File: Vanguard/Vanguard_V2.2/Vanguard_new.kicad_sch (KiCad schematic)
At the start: 75 parts, among them J1 USB_C_Receptacle_USB2.0_16P, J2 Conn_02x03_Pin, J3 Micro_SD_Card_Det1, J4 STARBOARD_SERVO, J5 PORTSIDE_SERVO, J6 Conn_01x02_Pin, Q1 BSS138, Q2 BSS138, Q3 BSS138, Q4 BSS138, U1 ATSAMD11D14A-M, U2 ATmega4809-A, U3 AT25DF641A-SH-T, U4 AP2112K-3.3, U5 BD1020HFV, U6 BNO086, U7 TXB0104D, U8 TPS61092, U9 MPM3610AGQV-P, Y1 32.768kHz

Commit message: Debugged some errors
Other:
- note added: "note servo isnt connected"
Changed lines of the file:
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@@
+		)
+	)
+	(text "note servo isnt connected"
+		(exclude_from_sim no)
+		(at 339.344 189.992 0)
+		(effects
+			(font
+				(size 1.27 1.27)
+			)
 		)
 	)

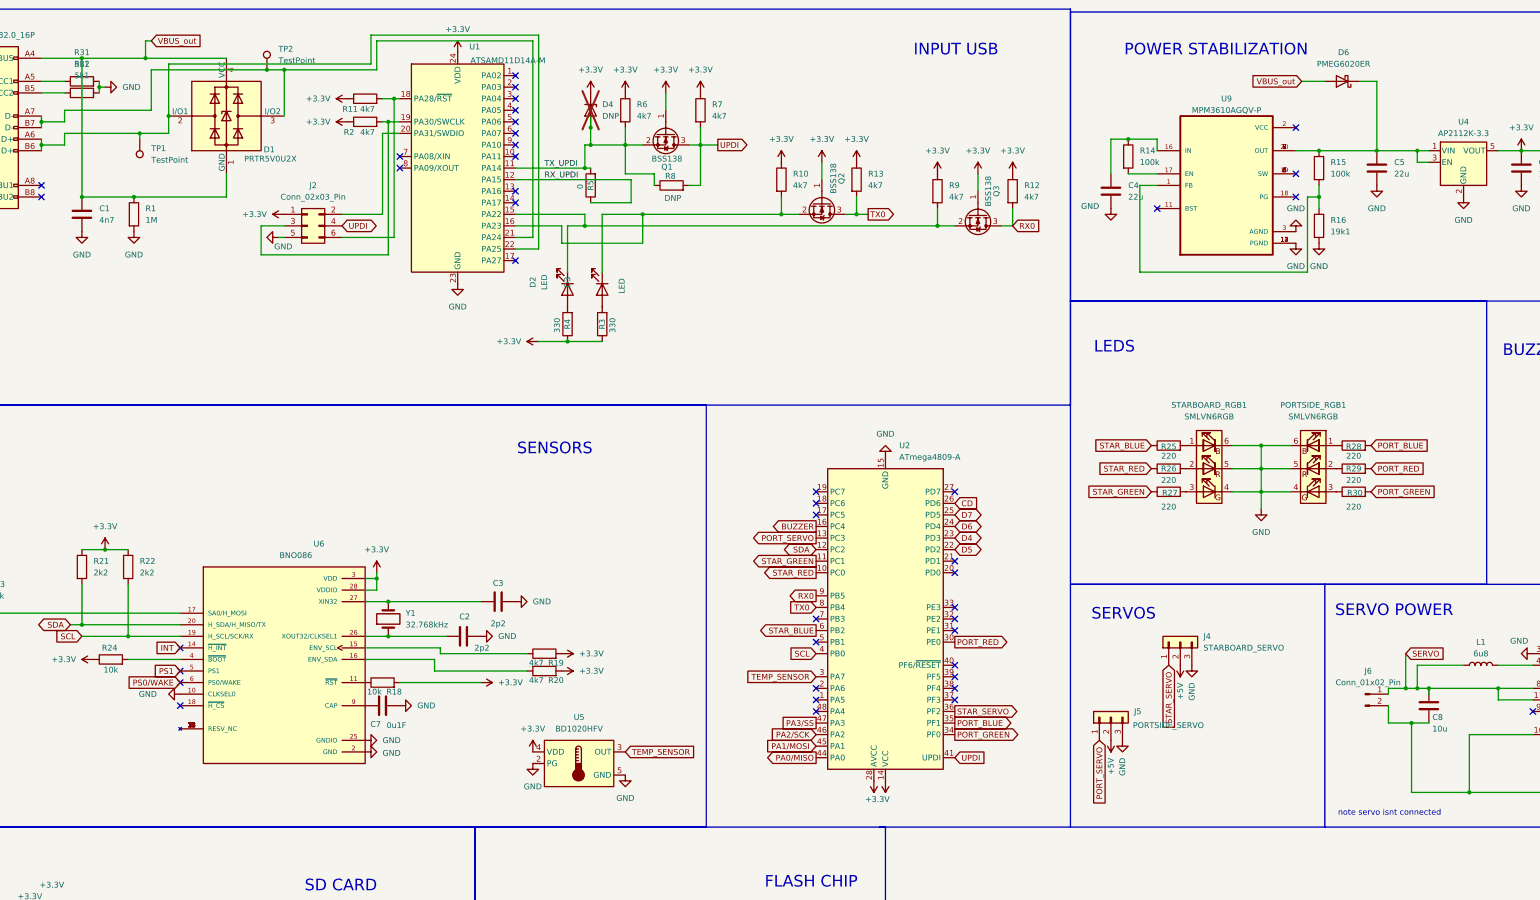
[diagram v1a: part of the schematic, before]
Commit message: Small erc changes as the pcb guys recommeded
@pchou05 @stygmatic what do you say? I am done with the sch but we still have some silly violations
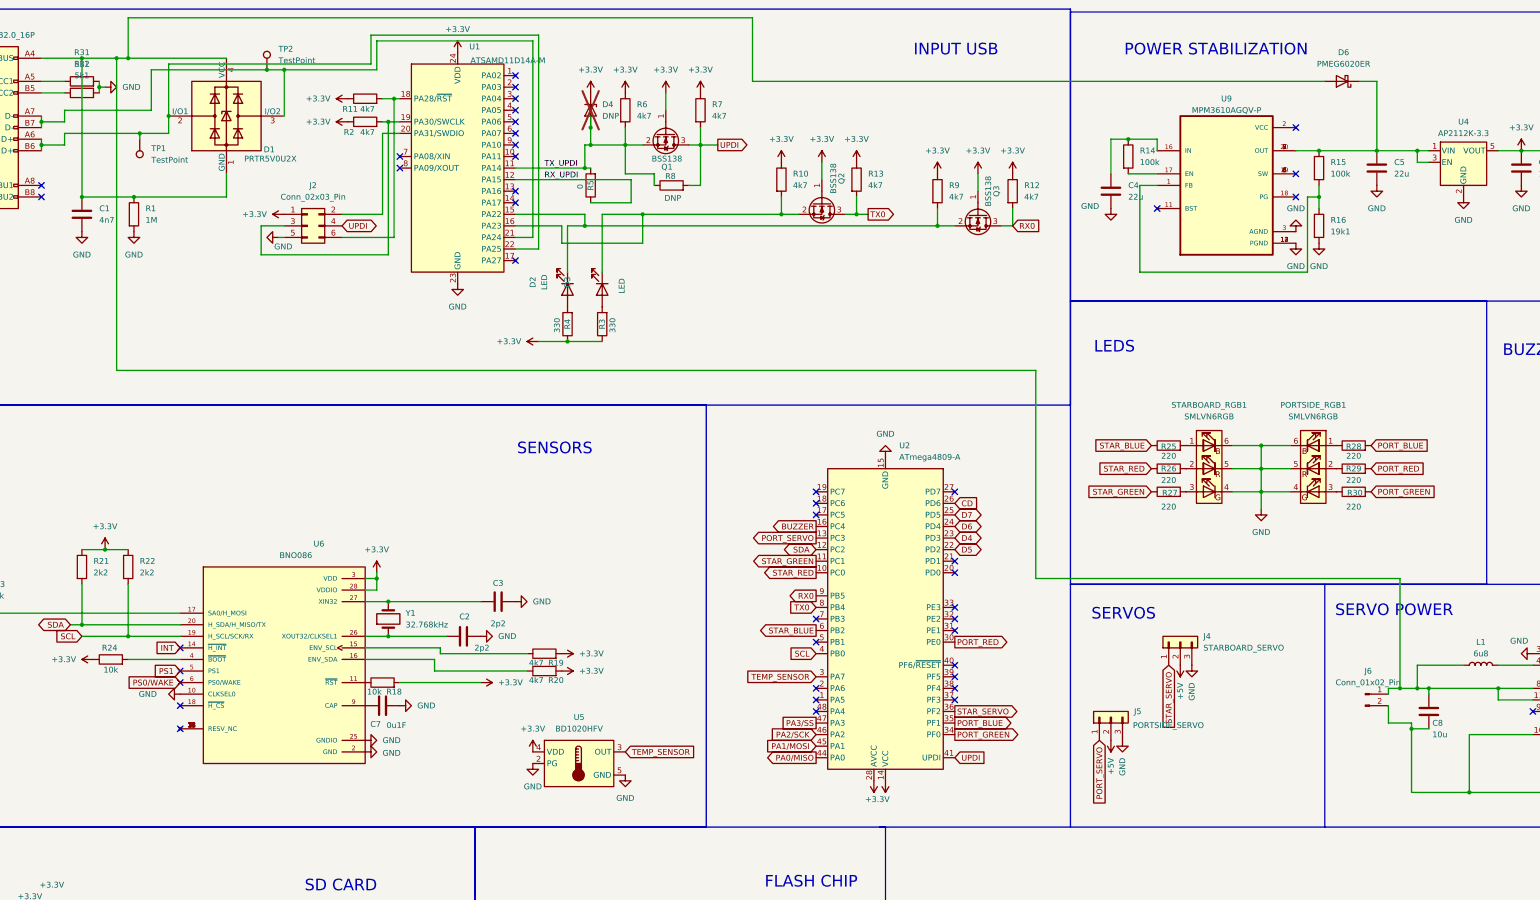
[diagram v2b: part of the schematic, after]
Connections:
- net VBUS_out is gone; now on an unnamed net: C1.1, D1.1 (GND), D1.4 (VCC), D6.2 (A), J1.A4 (VBUS), J1.A9 (VBUS), J1.B4 (VBUS), J1.B9 (VBUS), R1.1
- net SERVO: no longer names the net of C8.1, J6.1 (Pin_1), L1.1, U8.11 (EN), U8.8 (VBAT)
- no-connect marks 50 -> 51
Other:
- note removed: "note servo isnt connected"
- moved on the sheet: C8

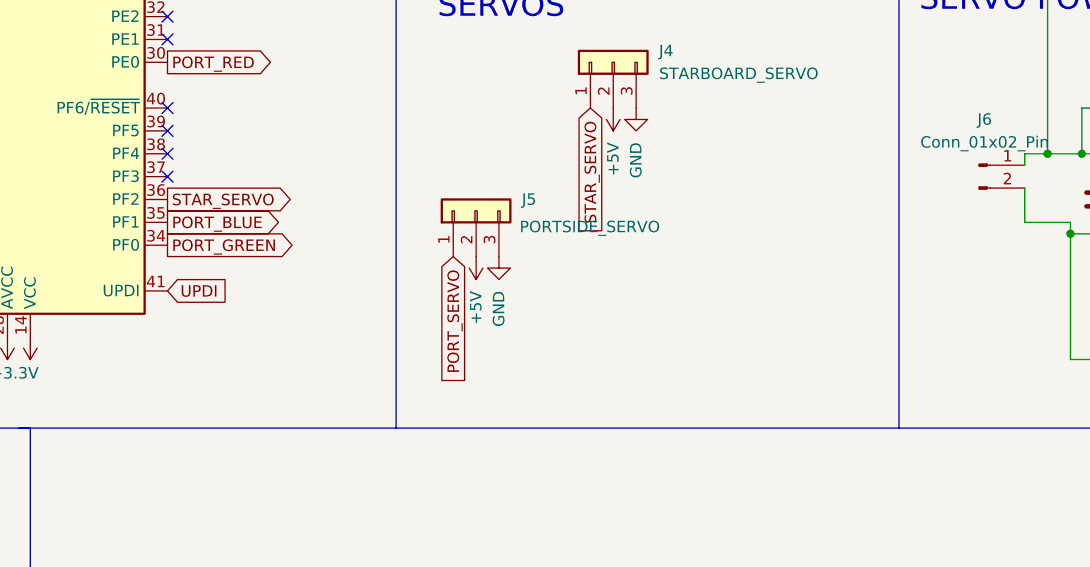
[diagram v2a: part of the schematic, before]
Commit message: ejec servo added
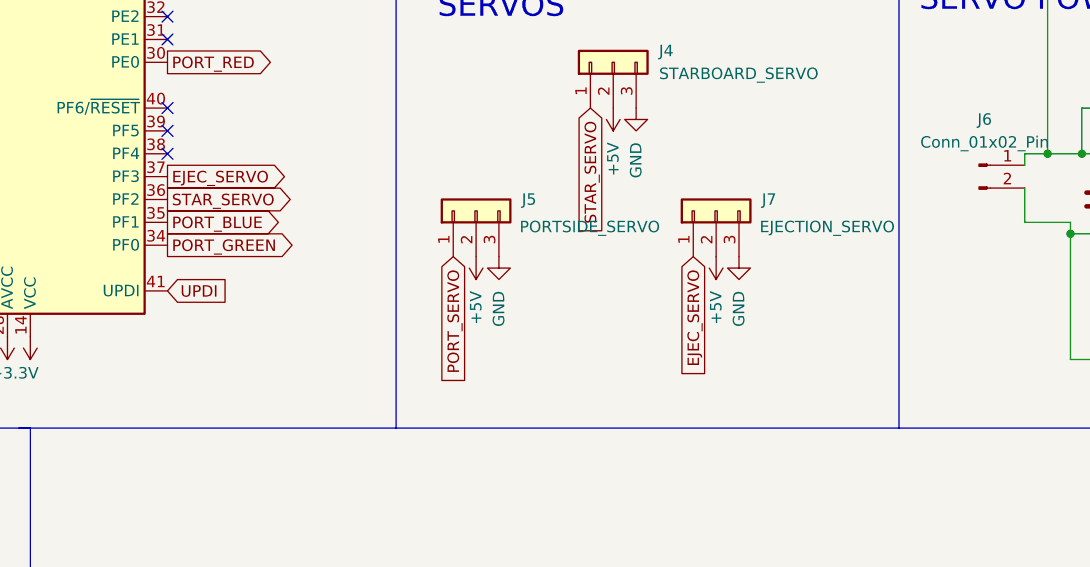
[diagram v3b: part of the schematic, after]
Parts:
- added J7: EJECTION_SERVO, Connector_PinHeader_2.54mm:PinHeader_1x03_P2.54mm_Vertical, symbol Connector_Generic:Conn_01x03
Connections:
- net +5V: now also J7.2 (Pin_2)
- net GND: now also J7.3 (Pin_3)
- net EJEC_SERVO: now reaches U2.37 (PF3)
- net EJEC_SERVO: now also J7.1 (Pin_1)
- no-connect marks 51 -> 50

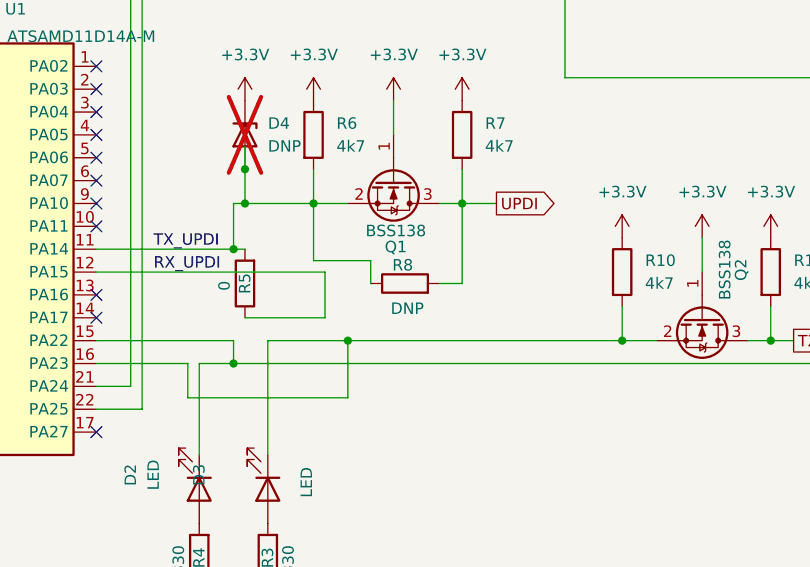
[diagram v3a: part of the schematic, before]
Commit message: implamented changes from embedded engineers
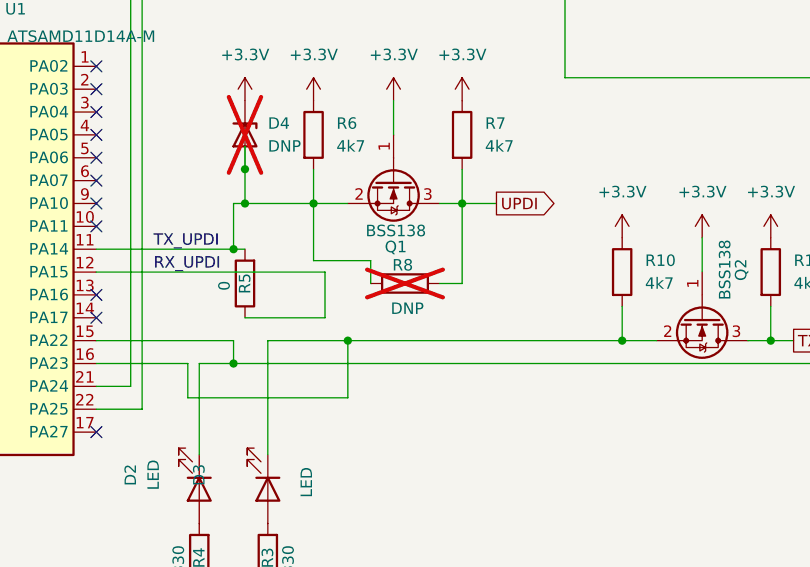
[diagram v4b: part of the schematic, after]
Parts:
- R8: now not fitted
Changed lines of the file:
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@@
 		(in_bom yes)
 		(on_board yes)
-		(dnp no)
+		(dnp yes)
 		(property "Reference" "R8"
 			(at 181.356 50.038 90)

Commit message: changes in labels, capacitors and buzzer-mosfet
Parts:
- added 2k2: R, symbol Device:R
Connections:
- net BUZZER: now also 2k2.1
- net GND: now also Q4.2 (S), 2k2.2; no longer Q4.3 (D)
- net POWER_STAB: now reaches C1.1, C8.1, D1.1 (GND), D1.4 (VCC), D6.2 (A), J1.A4 (VBUS), J1.A9 (VBUS), J1.B4 (VBUS), J1.B9 (VBUS), J6.1 (Pin_1), L1.1, R1.1, U8.11 (EN), U8.8 (VBAT)
- net at BZ1.2 (-): now also Q4.3 (D); no longer Q4.2 (S)

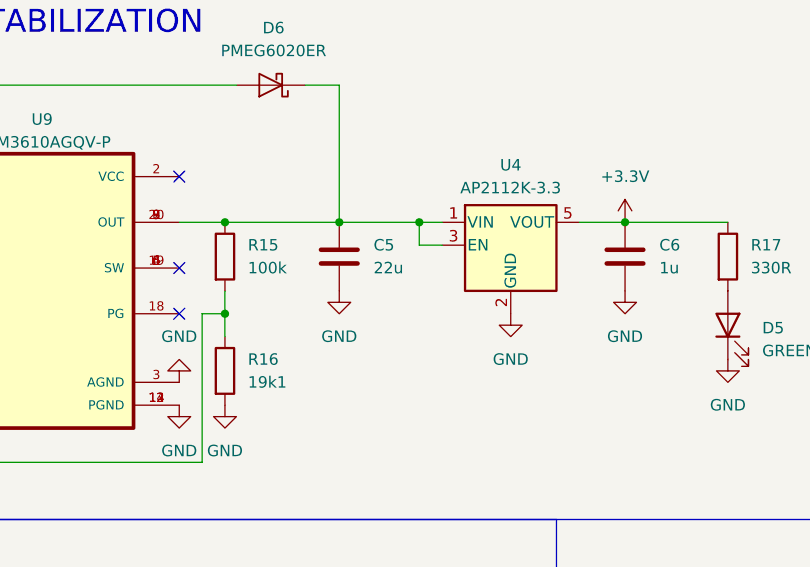
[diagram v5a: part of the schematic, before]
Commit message: added a 1uf cap to u4 input
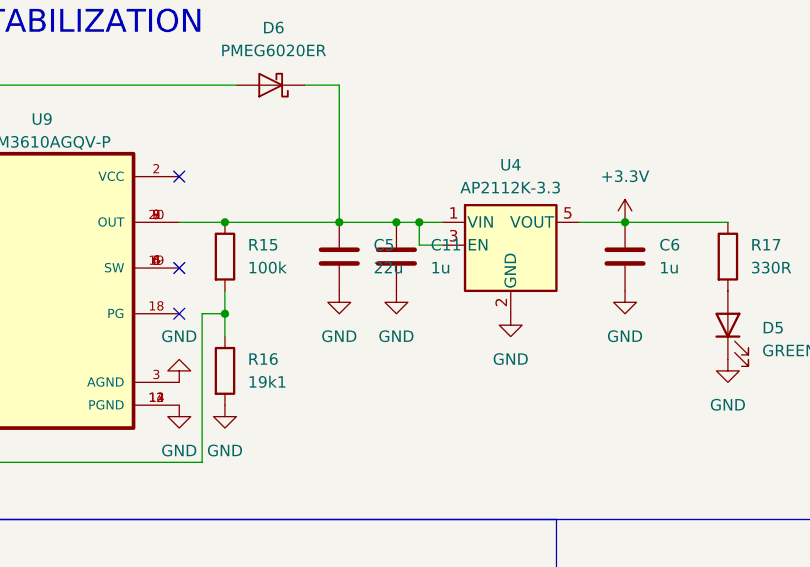
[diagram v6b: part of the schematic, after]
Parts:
- added C11: 1u, symbol Device:C
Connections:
- net GND: now also C11.2
- net at C5.1, D6.1 (K), R15.1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: now also C11.1
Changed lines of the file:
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@@
 	)
 	(junction
+		(at 342.9 44.45)
+		(diameter 0)
+		(color 0 0 0 0)
+	)
+	(junction
 		(at 377.19 114.3)
 		(diameter 0)
@@
 	(wire
 		(pts
-			(xy 336.55 44.45) (xy 345.44 44.45)
+			(xy 336.55 44.45) (xy 342.9 44.45)
 		)
 		(stroke
@@
 	(wire
 		(pts
+			(xy 342.9 44.45) (xy 345.44 44.45)
+		)
+		(stroke
+			(width 0)
+			(type default)
+		)
+	)
+	(wire
+		(pts
 			(xy 191.77 43.18) (xy 187.96 43.18)
 		)
@@
 	(symbol
 		(lib_id "power:GND")
+		(at 342.9 52.07 0)
+		(unit 1)
+		(exclude_from_sim no)
+		(in_bom yes)
+		(on_board yes)
+		(dnp no)
+		(fields_autoplaced yes)
+		(property "Reference" "#PWR073"
+			(at 342.9 58.42 0)
+			(effects
+				(font
+					(size 1.27 1.27)
+				)
+				(hide yes)
+			)
+		)
+		(property "Value" "GND"
+			(at 342.9 57.15 0)
+			(effects
+				(font
+					(size 1.27 1.27)
+				)
+			)
+		)
+		(property "Footprint" ""
+			(at 342.9 52.07 0)
+			(effects
+				(font
+					(size 1.27 1.27)
+				)
+				(hide yes)
+			)
+		)
+		(property "Datasheet" ""
+			(at 342.9 52.07 0)
+			(effects
+				(font
+					(size 1.27 1.27)
+				)
+				(hide yes)
+			)
+		)
+		(property "Description" "Power symbol creates a global label with name \"GND\" , ground"
+			(at 342.9 52.07 0)
+			(effects
+				(font
+					(size 1.27 1.27)
+				)
+				(hide yes)
+			)
+		)
+		(pin "1"
+		)
+		(instances
+			(project ""
+				(path "/972fbf12-2dcd-4fdf-b1c9-8a2880c46640"
+					(reference "#PWR073")
+					(unit 1)
+				)
+			)
+		)
+	)
+	(symbol
+		(lib_id "power:GND")
 		(at 318.77 64.77 0)
 		(unit 1)
@@
 					(unit 1)
 				)
+			)
+		)
+	)
+	(symbol
+		(lib_id "Device:C")
+		(at 342.9 48.26 0)
+		(unit 1)
+		(exclude_from_sim no)
+		(in_bom yes)
+		(on_board yes)
+		(dnp no)
+		(fields_autoplaced yes)
+		(property "Reference" "C11"
+			(at 346.71 46.9899 0)
+			(effects
+				(font
+					(size 1.27 1.27)
+				)
+				(justify left)
+			)
+		)
+		(property "Value" "1u"
+			(at 346.71 49.5299 0)
+			(effects
+				(font
+					(size 1.27 1.27)
+				)
+				(justify left)
+			)
+		)
+		(property "Footprint" ""
+			(at 343.8652 52.07 0)
+			(effects
+				(font
+					(size 1.27 1.27)
+				)
+				(hide yes)
+			)
+		)
+		(property "Datasheet" "~"
+			(at 342.9 48.26 0)
+			(effects
+				(font
+					(size 1.27 1.27)
+				)
+				(hide yes)
+			)
+		)
+		(property "Description" "Unpolarized capacitor"
+			(at 342.9 48.26 0)
+			(effects
+				(font
+					(size 1.27 1.27)
+				)
+				(hide yes)
+			)
+		)
+		(pin "1"
+		)
+		(pin "2"
+		)
+		(instances
+			(project ""
+				(path "/972fbf12-2dcd-4fdf-b1c9-8a2880c46640"
+					(reference "C11")
+					(unit 1)
+				)

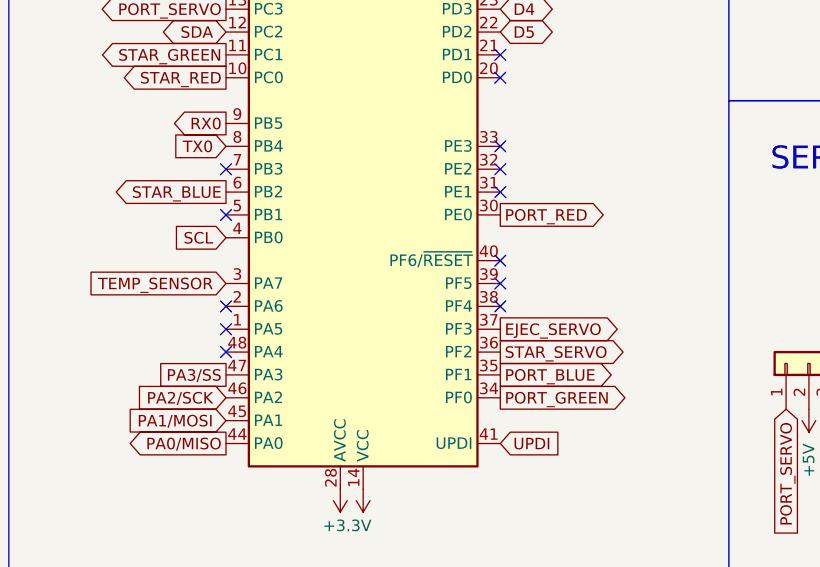
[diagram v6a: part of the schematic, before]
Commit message: moved label "EJEC_SERVO" FROM pf3 to pf4 in MC and moved "scl" LABEL from PB0 TO pf3 and added a dnp in PB0
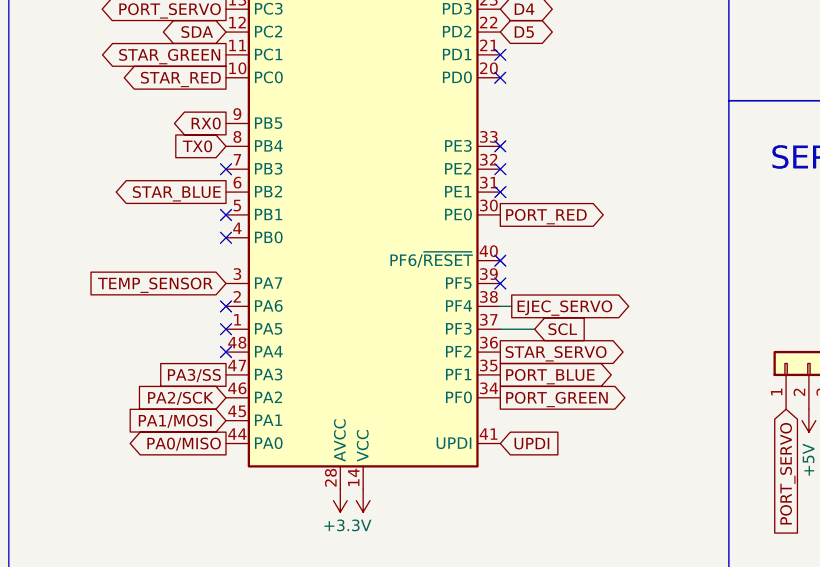
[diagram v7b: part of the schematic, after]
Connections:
- net EJEC_SERVO: now also U2.38 (PF4); no longer U2.37 (PF3)
- net SCL: now also U2.37 (PF3); no longer U2.4 (PB0)
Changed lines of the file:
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@@
 	)
 	(no_connect
+		(at 213.36 154.94)
+	)
+	(no_connect
 		(at 391.16 165.1)
 	)
@@
 	)
 	(no_connect
-		(at 243.84 162.56)
-	)
-	(no_connect
 		(at 243.84 134.62)
 	)
@@
 	(wire
 		(pts
+			(xy 245.11 162.56) (xy 243.84 162.56)
+		)
+		(stroke
+			(width 0)
+			(type default)
+		)
+	)
+	(wire
+		(pts
 			(xy 52.07 139.7) (xy 52.07 148.59)
 		)
@@
 	(wire
 		(pts
+			(xy 247.65 165.1) (xy 243.84 165.1)
+		)
+		(stroke
+			(width 0)
+			(type default)
+		)
+	)
+	(wire
+		(pts
 			(xy 91.44 67.31) (xy 91.44 60.96)
 		)
@@
 	(global_label "EJEC_SERVO"
 		(shape output)
-		(at 243.84 165.1 0)
+		(at 245.11 162.56 0)
 		(fields_autoplaced yes)
 		(effects
@@
 		)
 		(property "Intersheetrefs" "${INTERSHEET_REFS}"
-			(at 258.376 165.1 0)
+			(at 259.646 162.56 0)
 			(effects
 				(font
@@
 		)
 	)
-	(global_label "SCL"
-		(shape input)
-		(at 213.36 154.94 180)
-		(fields_autoplaced yes)
-		(effects
-			(font
-				(size 1.27 1.27)
-			)
-			(justify right)
-		)
-		(property "Intersheetrefs" "${INTERSHEET_REFS}"
-			(at 206.8672 154.94 0)
-			(effects
-				(font
-					(size 1.27 1.27)
-				)
-				(justify right)
-				(hide yes)
-			)
-		)
-	)
 	(global_label "CD"
 		(shape input)
@@
 				(hide yes)
 			)
+		)
+	)
+	(global_label "SCL"
+		(shape input)
+		(at 247.65 165.1 0)
+		(fields_autoplaced yes)
+		(effects
+			(font
+				(size 1.27 1.27)
+			)
+			(justify left)
+		)
+		(property "Intersheetrefs" "${INTERSHEET_REFS}"
+			(at 254.1428 165.1 0)
+			(effects
+				(font
+					(size 1.27 1.27)
+				)
+				(justify left)
+				(hide yes)
+			)
